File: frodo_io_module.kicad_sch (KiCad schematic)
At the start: 2 parts, among them J1 Molex MicroFit 2x3, J2 Molex MicroFit 2x3

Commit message: basic microcontroller peripherals
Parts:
- added C1, C2, C3, C4, C9: 100n, symbol Device:C
- added C10, C11: 10p, symbol Device:C
- added C12, C13: 22u, symbol Device:C
- added C5: 10u, symbol Device:C
- added C6: 10n, symbol Device:C
- added C7, C8: 1u, symbol Device:C
- added D1: RED, symbol Device:LED
- added FB1: 120R, symbol Device:FerriteBead
- added J1, J3, J4: Conn_01x04_Pin, symbol Connector:Conn_01x04_Pin
- added J2: USB_B_Micro, symbol Connector:USB_B_Micro
- added R1: 10k, symbol Device:R
- added R2, R4, R5: 1K5, symbol Device:R
- added R3: R, symbol Device:R
- added SW1: SW_SPDT, symbol Switch:SW_SPDT
- added U1: STM32F072RBT6, Package_QFP:LQFP-64_10x10mm_P0.5mm, symbol MCU_ST_STM32F0:STM32F072RBTx
- added U2: AMS1117-3.3, Package_TO_SOT_SMD:SOT-223-3_TabPin2, symbol Regulator_Linear:AMS1117-3.3
- added Y1: 8MHz, symbol Device:Crystal_GND24
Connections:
- net GND: now also C1.2, C10.2, C11.2, C12.2, C13.2, C2.2, C3.2, C4.2, C5.2, C6.2, C7.2, C8.2, C9.2, J1.4 (Pin_4), J2.5 (GND), J3.4 (Pin_4), J4.4 (Pin_4), R3.2, SW1.1 (A), U1.12 (VSSA), U1.18 (VSS), U1.31 (VSS), U1.47 (VSS), U1.63 (VSS), U2.1 (GND), Y1.2, Y1.4
- new net +3.3V: C1.1, C13.1, C2.1, C3.1, C4.1, C5.1, C8.1, D1.2 (A), FB1.1, J1.1 (Pin_1), J3.1 (Pin_1), J4.1 (Pin_1), R2.1, R4.1, R5.1, SW1.3 (C), U1.1 (VBAT), U1.19 (VDD), U1.32 (VDD), U1.64 (VDD), U2.2 (VO)
- new net +3.3VA: C6.1, C7.1, FB1.2, U1.13 (VDDA)
- new net BOOTO: R1.2, U1.60 (BOOT0)
- new net HSE_IN: C10.1, U1.5 (PF0), Y1.1
- new net HSE_OUT: C11.1, U1.6 (PF1), Y1.3
- new net I2C2_SCL: J3.2 (Pin_2), R4.2, U1.29 (PB10)
- new net I2C2_SDA: J3.3 (Pin_3), R5.2, U1.30 (PB11)
- new net NRST: C9.1, U1.7 (NRST)
- new net PWR_LED_K: D1.1 (K), R3.1
- new net SWCLK: J1.2 (Pin_2), J1.3 (Pin_3), U1.46 (PA13), U1.49 (PA14)
- new net SW_BOOTO: R1.1, SW1.2 (B)
- new net USART1_RX: J4.3 (Pin_3), U1.59 (PB7)
- new net USART1_TX: J4.2 (Pin_2), U1.58 (PB6)
- new net USB_D+: J2.3 (D+), R2.2, U1.45 (PA12)
- new net USB_D-: J2.2 (D-), U1.44 (PA11)
- new net VBUS: C12.1, J2.1 (VBUS), U2.3 (VI)
- no-connect marks 0 -> 42

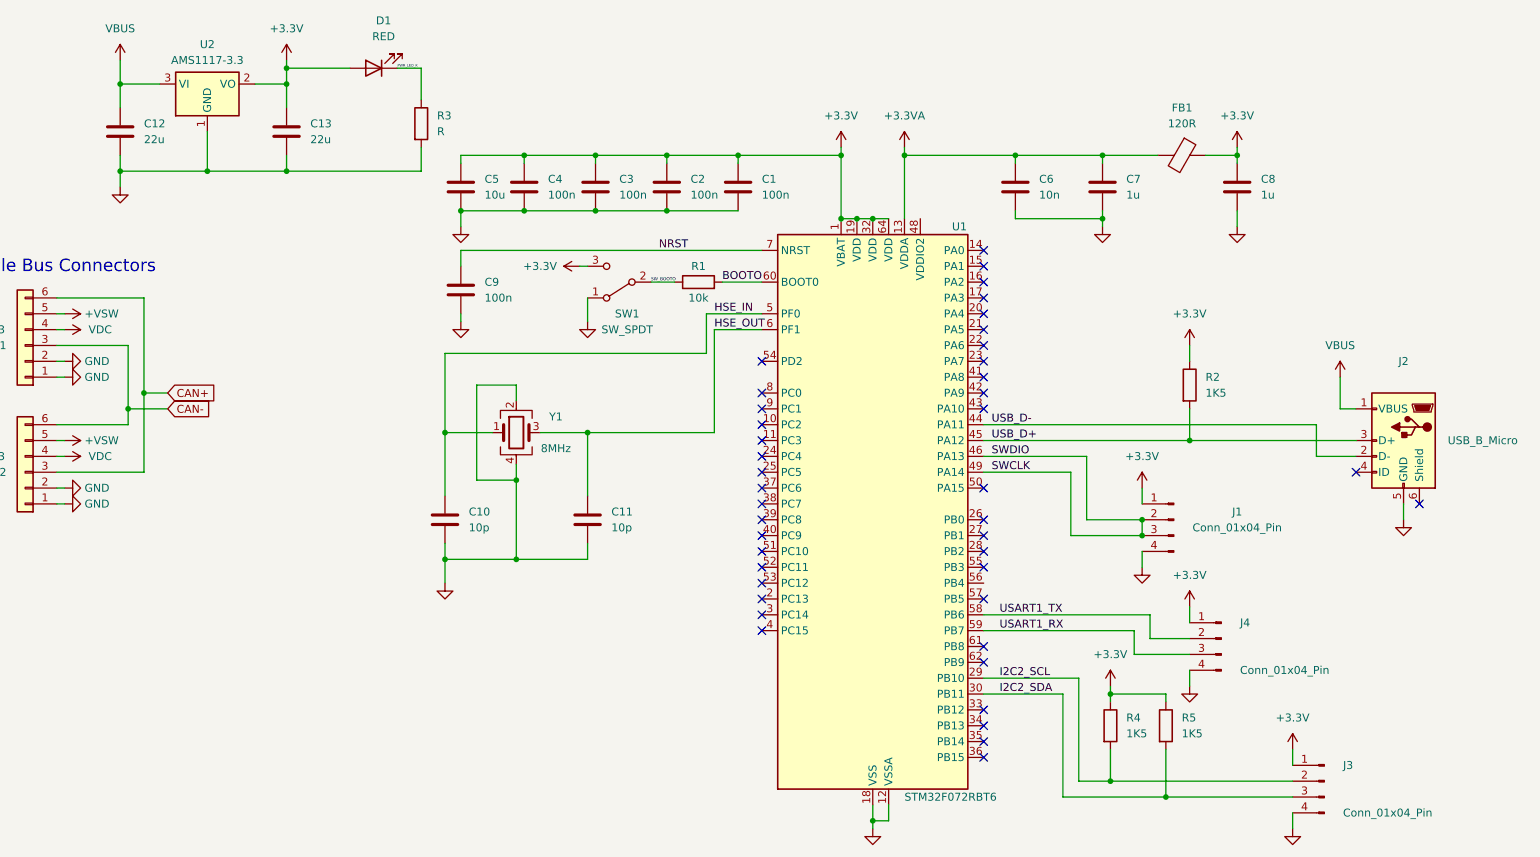
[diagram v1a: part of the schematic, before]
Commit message: USART Pin Configuration
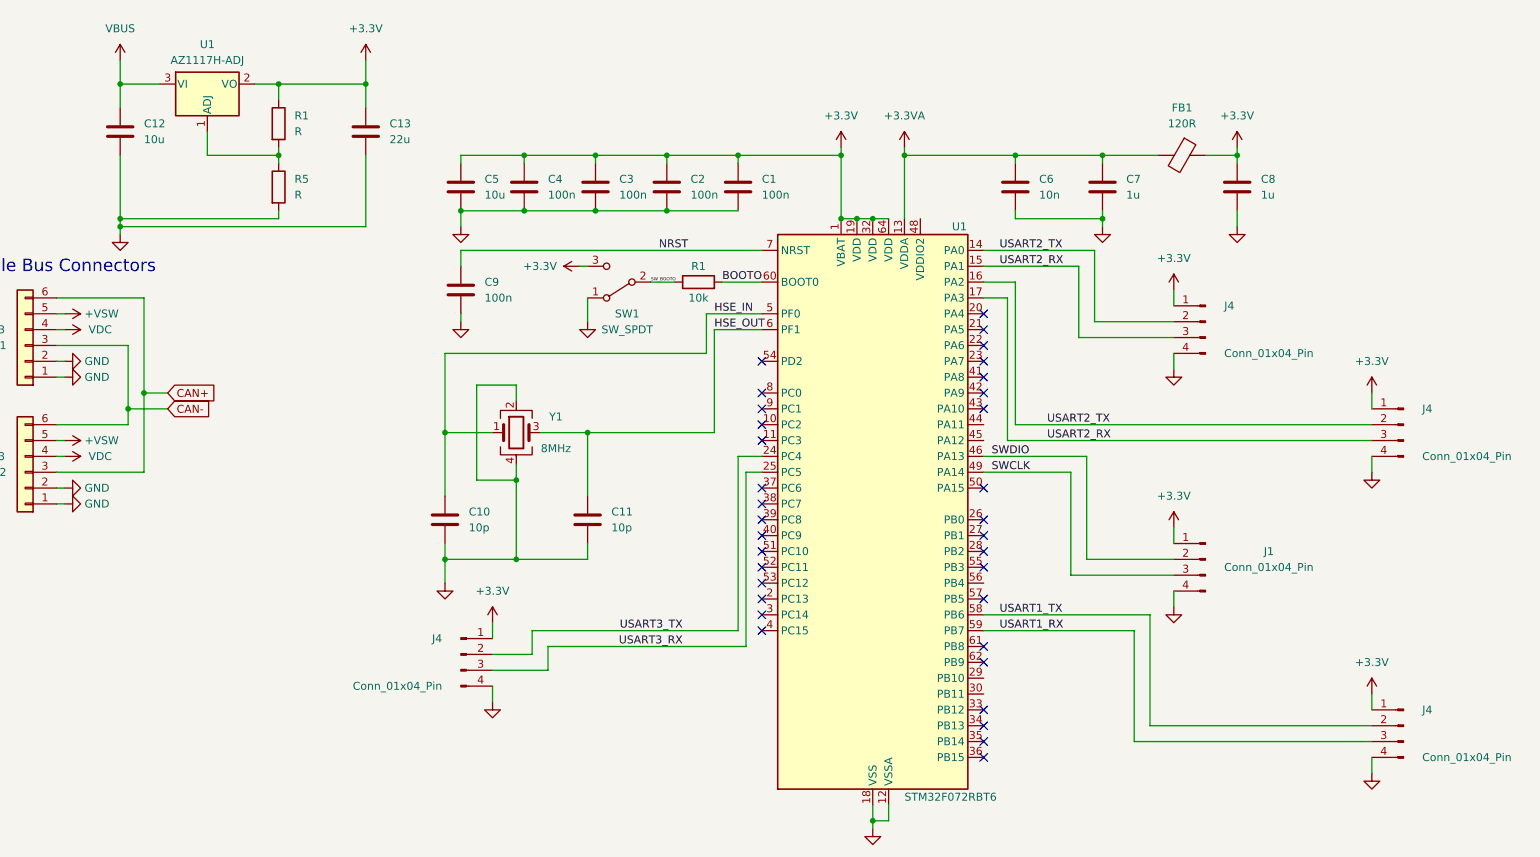
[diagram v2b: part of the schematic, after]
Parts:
- removed D1: RED, symbol Device:LED
- removed J2: USB_B_Micro, symbol Connector:USB_B_Micro
- removed J3: Conn_01x04_Pin, symbol Connector:Conn_01x04_Pin
- removed R2, R4: 1K5, symbol Device:R
- removed R3: R, symbol Device:R
- removed U2: AMS1117-3.3, Package_TO_SOT_SMD:SOT-223-3_TabPin2, symbol Regulator_Linear:AMS1117-3.3
- added J4 (x3): Conn_01x04_Pin, symbol Connector:Conn_01x04_Pin
- added R1: R, symbol Device:R
- added U1: AZ1117H-ADJ, Package_TO_SOT_SMD:SOT-223-3_TabPin2, symbol Regulator_Linear:AZ1117H-ADJ
- C12: value 22u -> 10u
- R5: value 1K5 -> R
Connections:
- net +3.3V: now also J4.1 (Pin_1), J4.1 (Pin_1), J4.1 (Pin_1), R1.1, U1.2 (VO); no longer R5.1
- net GND: now also R5.2, J4.4 (Pin_4), J4.4 (Pin_4), J4.4 (Pin_4)
- net SWCLK: no longer J1.2 (Pin_2), U1.46 (PA13)
- net VBUS: now also U1.3 (VI)
- net USART2_TX: now reaches U1.14 (PA0)
- net USART2_TX: now also U1.16 (PA2), J4.2 (Pin_2), J4.2 (Pin_2)
- net USART2_RX: now reaches U1.15 (PA1)
- net USART2_RX: now also U1.17 (PA3), J4.3 (Pin_3), J4.3 (Pin_3)
- net USART3_TX: now reaches U1.24 (PC4)
- net USART3_TX: now also J4.2 (Pin_2)
- net USART3_RX: now reaches U1.25 (PC5)
- net USART3_RX: now also J4.3 (Pin_3)
- net I2C2_SCL: no longer names the net of U1.29 (PB10)
- net I2C2_SDA: no longer names the net of U1.30 (PB11)
- net I2C2_SDA: no longer R5.2
- net USB_D+: no longer names the net of U1.45 (PA12)
- net USB_D-: no longer names the net of U1.44 (PA11)
- new net: R1.2, R5.1, U1.1 (ADJ)
- new net SWDIO: J1.2 (Pin_2), U1.46 (PA13)
- no-connect marks 42 -> 34
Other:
- moved on the sheet: C13, J1, J4

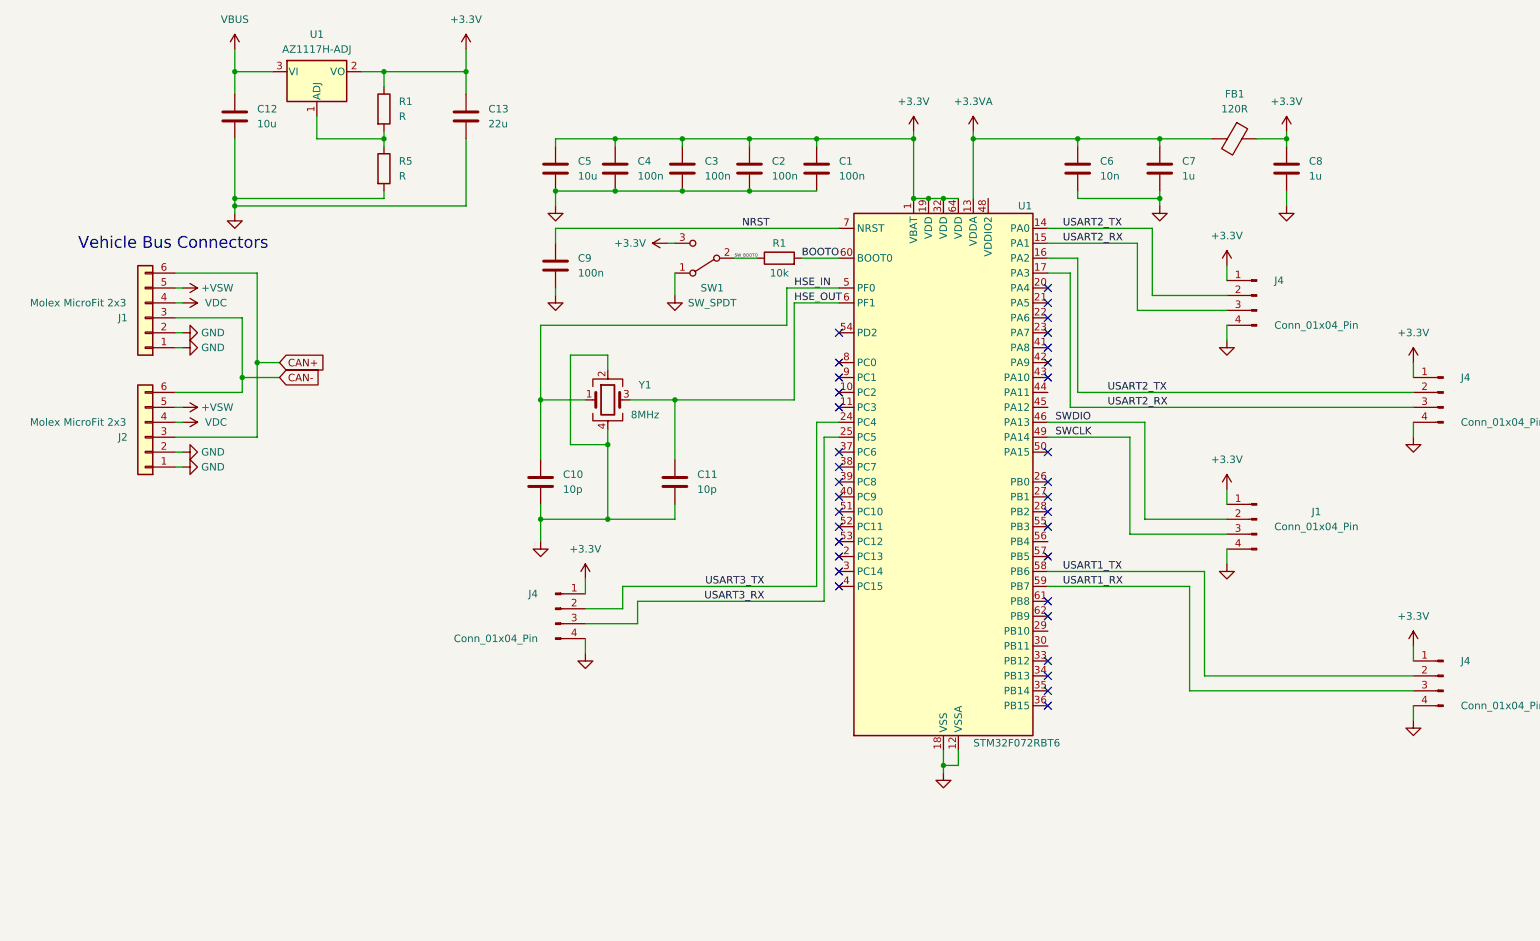
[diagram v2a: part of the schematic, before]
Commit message: voltage regulator addition
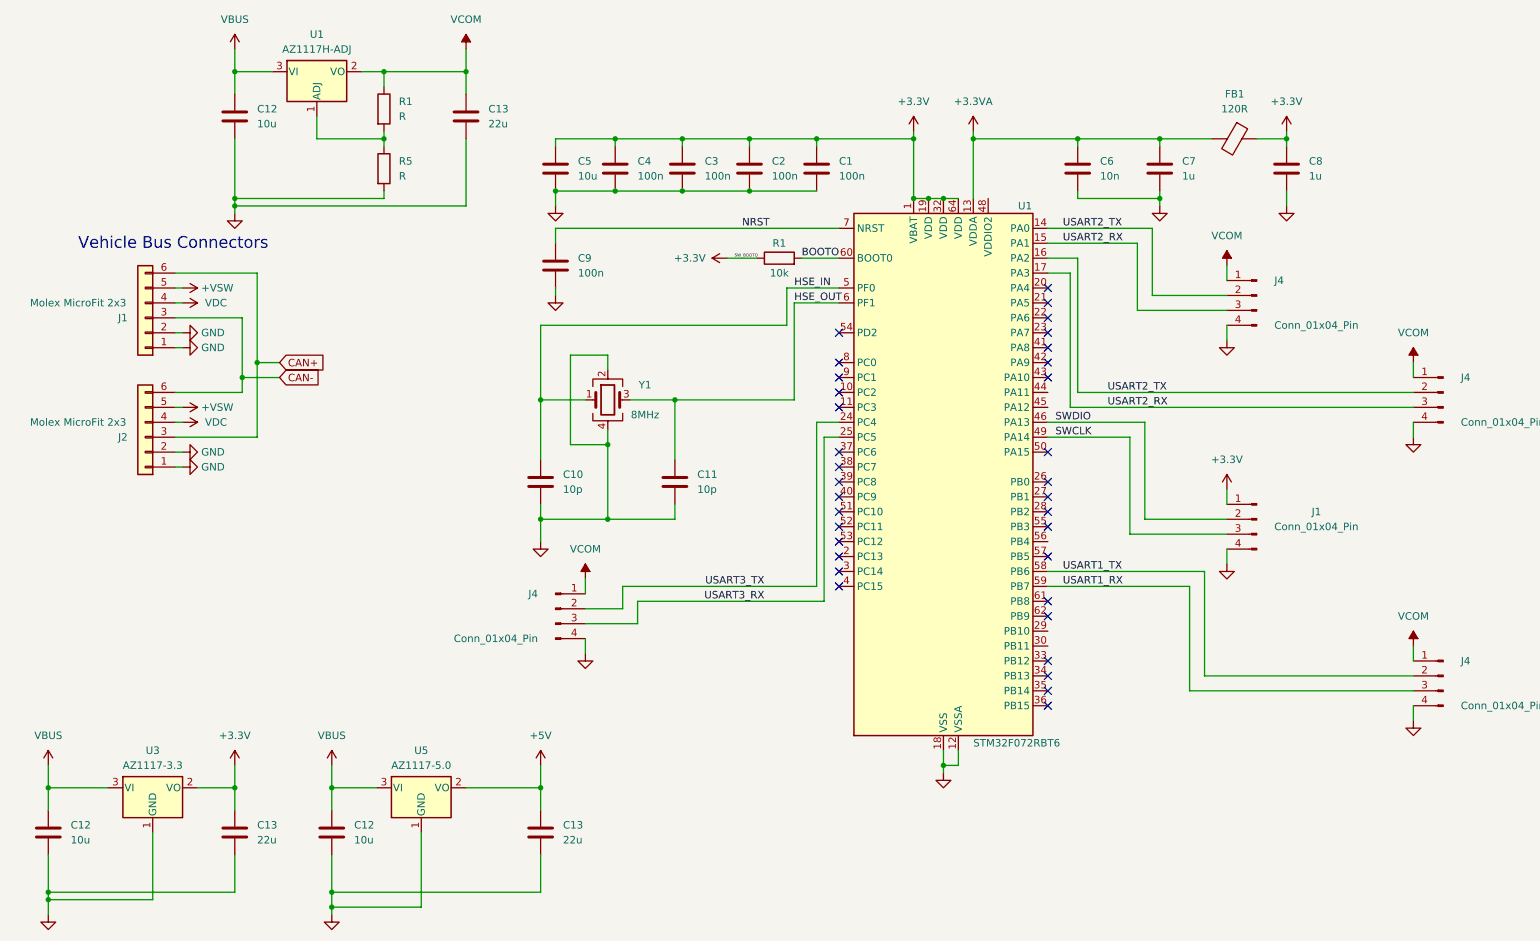
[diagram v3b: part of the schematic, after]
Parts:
- removed SW1: SW_SPDT, symbol Switch:SW_SPDT
- added C12 (x2): 10u, symbol Device:C
- added C13 (x2): 22u, symbol Device:C
- added U3: AZ1117-3.3, symbol Regulator_Linear:AZ1117-3.3
- added U5: AZ1117-5.0, symbol Regulator_Linear:AZ1117-5.0
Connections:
- net SW_BOOTO is gone; now on net +3.3V: R1.1
- net +3.3V: now also C13.1, U3.2 (VO); no longer C13.1, J4.1 (Pin_1), J4.1 (Pin_1), J4.1 (Pin_1), J4.1 (Pin_1), R1.1, U1.2 (VO)
- net GND: now also C12.2, C12.2, C13.2, C13.2, U3.1 (GND), U5.1 (GND)
- net VBUS: now also C12.1, C12.1, U3.3 (VI), U5.3 (VI)
- new net +5V: C13.1, U5.2 (VO)
- new net VCOM: C13.1, J4.1 (Pin_1), J4.1 (Pin_1), J4.1 (Pin_1), J4.1 (Pin_1), R1.1, U1.2 (VO)
